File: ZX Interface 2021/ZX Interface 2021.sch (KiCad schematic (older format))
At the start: 56 parts, among them J1 JOYSTICK 2, J2 JOYSTICK 1, J3 BA14_HI, J4 Extended Cartridge Port, J5 JOYSTICK_EN, M1 Mounting, M2 Mounting, M3 Mounting, M4 Mounting, M5 Mounting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

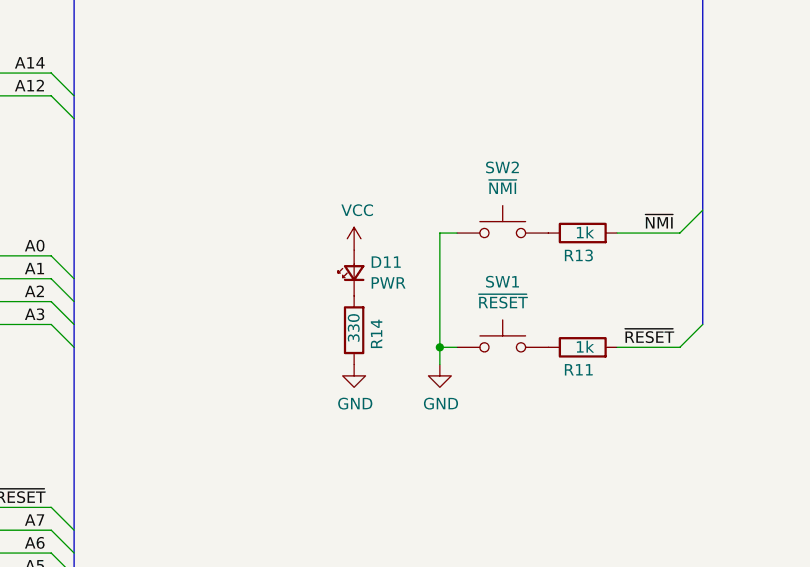
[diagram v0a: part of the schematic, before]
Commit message: Tweaked interface title
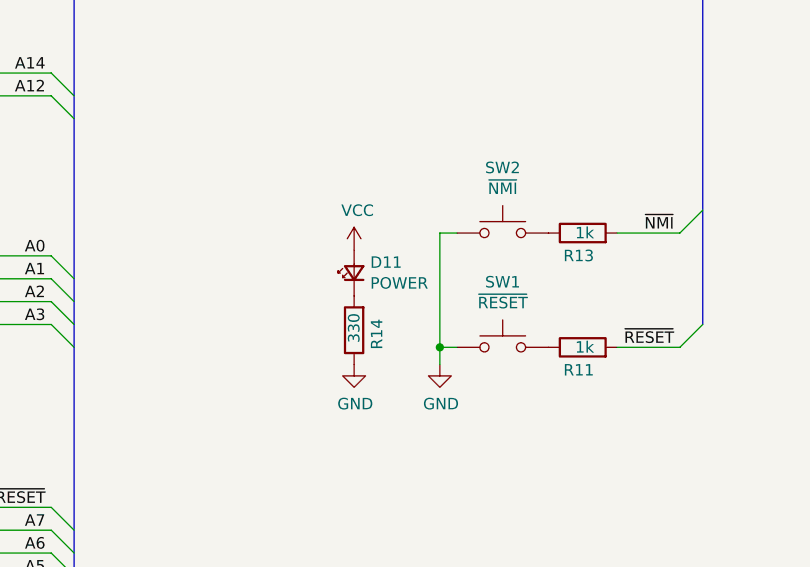
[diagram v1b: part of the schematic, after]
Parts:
- D11: value PWR -> POWER
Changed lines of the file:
@@
 Title "ZX Interface 2.021"
 Date ""
-Rev ""
+Rev "B"
 Comp ""
 Comment1 ""
@@
 P 4675 2050
 F 0 "D11" V 4721 1980 50  0000 R CNN
-F 1 "PWR" V 4630 1980 50  0000 R CNN
+F 1 "POWER" V 4630 1980 50  0000 R CNN
 F 2 "LED_THT:LED_D5.0mm" V 4675 2050 50  0001 C CNN
 F 3 "~" V 4675 2050 50  0001 C CNN
